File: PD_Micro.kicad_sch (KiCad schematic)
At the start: 43 parts, among them J3 Conn_01x02, Q1 DMP3017SFK, Q2 DTC143E, SW1 SW_DPST_x2, SW2 SW_Push, SW4 SW_DPST_x2, SW5 SW_DIP_x06, SW6 SW_Push, U1 TPS62175DQC, U2 SRV05-4, U3 Pico, U4 FUSB302BMPX, U5 ACS723xMATR-10AB, U6 oledSym

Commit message: pcb
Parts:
- SW2, SW6: footprint Button_Switch_SMD:SW_SPST_TL3305C -> Button_Switch_SMD:SW_SPST_TL3305B
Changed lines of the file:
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@@
       (effects (font (size 1.27 1.27)))
     )
-    (property "Footprint" "Button_Switch_SMD:SW_SPST_TL3305C" (at 118.11 144.78 0)
+    (property "Footprint" "Button_Switch_SMD:SW_SPST_TL3305B" (at 118.11 144.78 0)
       (effects (font (size 1.27 1.27)) hide)
     )
@@
       (effects (font (size 1.27 1.27)))
     )
-    (property "Footprint" "Button_Switch_SMD:SW_SPST_TL3305C" (at 116.84 134.62 0)
+    (property "Footprint" "Button_Switch_SMD:SW_SPST_TL3305B" (at 116.84 134.62 0)
       (effects (font (size 1.27 1.27)) hide)
     )

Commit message: silk
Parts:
- renumbered C12 to C1, C13 to C10, C1 to C11, C15 to C12, C6 to C2, C16 to C3, C8 to C4, C17 to C5, C7 to C6, C4 to C7, C3 to C8, C2 to C9, H3 to H1, H1 to H2, H4 to H3, H2 to H4, J3 to J1, R9 to R1, R8 to R2, R7 to R3, R12 to R4, R4 to R5, R1 to R6, R2 to R7, R3 to R8, R11 to R9, SW5 to SW1, SW1 to SW2, SW6 to SW3, SW2 to SW4, SW4 to SW5, U2 to U1, U3 to U2, U1 to U3
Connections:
- net GND: now also U2.33 (AGND)

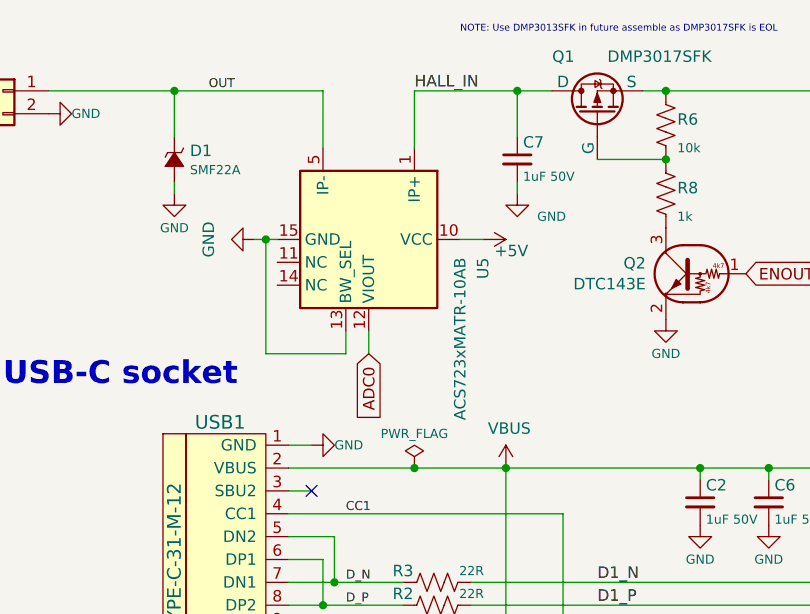
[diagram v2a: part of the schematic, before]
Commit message: bevore silkscreen delete
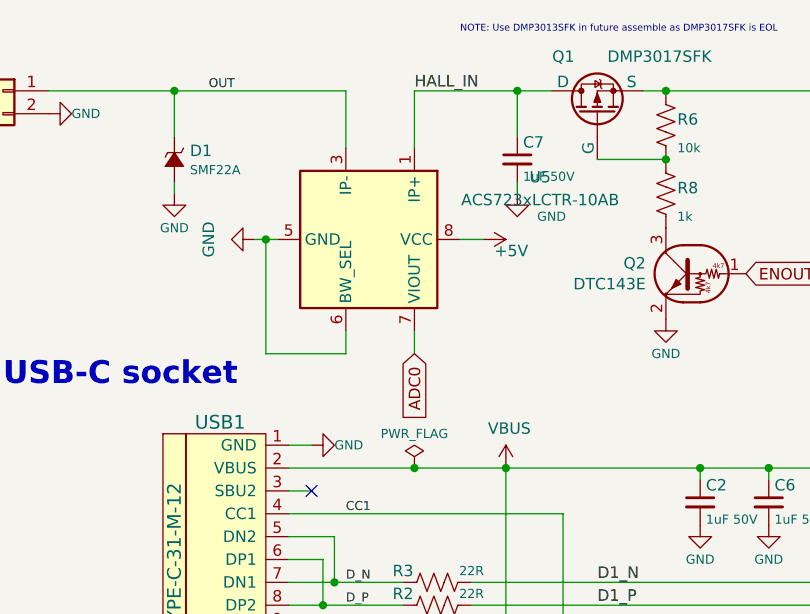
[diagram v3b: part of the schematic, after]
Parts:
- removed U5: ACS723xMATR-10AB, Package_SO:SOIC-16W_7.5x10.3mm_P1.27mm, symbol Sensor_Current:ACS723xMATR-10AB
- added U5: ACS723xLCTR-10AB, Package_SO:SOIC-8_3.9x4.9mm_P1.27mm, symbol Sensor_Current:ACS723xLCTR-10AB
- U6: footprint SSD1306:128x64OLED -> OLED094:SSD1306_0.96_Oled
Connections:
- net +5V: now also U5.8 (VCC)
- net ADC0: now also U5.7 (VIOUT)
- net GND: now also U5.5 (GND), U5.6 (BW_SEL)
- net HALL_IN: now also U5.1 (IP+), U5.2 (IP+)
- net OUT: now also U5.3 (IP-), U5.4 (IP-)
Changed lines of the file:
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@@
     (stroke (width 0) (type default))
   )
-  (wire (pts (xy 49.53 22.86) (xy 66.04 22.86))
+  (wire (pts (xy 49.53 22.86) (xy 68.58 22.86))
     (stroke (width 0) (type default))
   )
@@
     (stroke (width 0) (type default))
   )
-  (wire (pts (xy 66.04 29.21) (xy 66.04 22.86))
+  (wire (pts (xy 68.58 29.21) (xy 68.58 22.86))
     (stroke (width 0) (type default))
   )
@@
     (stroke (width 0) (type default))
   )
-  (wire (pts (xy 71.12 49.53) (xy 71.12 52.07))
+  (wire (pts (xy 76.2 49.53) (xy 76.2 52.07))
     (stroke (width 0) (type default))
   )
@@
     )
   )
-  (global_label "ADC0" (shape input) (at 71.12 52.07 270) (fields_autoplaced)
+  (global_label "ADC0" (shape input) (at 76.2 52.07 270) (fields_autoplaced)
     (effects (font (size 1.27 1.27)) (justify right))
-    (property "Intersheetrefs" "${INTERSHEET_REFS}" (at 71.1994 59.2323 90)
+    (property "Intersheetrefs" "${INTERSHEET_REFS}" (at 76.2794 59.2323 90)
       (effects (font (size 1.27 1.27)) (justify right) hide)
     )
@@
       (effects (font (size 1.27 1.27)) (justify left))
     )
-    (property "Footprint" "SSD1306:128x64OLED" (at 245.11 142.24 0)
+    (property "Footprint" "OLED094:SSD1306_0.96_Oled" (at 245.11 142.24 0)
       (effects (font (size 1.27 1.27)) hide)
     )
@@
     )
   )
-  (symbol (lib_id "Sensor_Current:ACS723xMATR-10AB") (at 71.12 39.37 270) (unit 1)
+  (symbol (lib_id "Sensor_Current:ACS723xLCTR-10AB") (at 71.12 39.37 270) (unit 1)
     (in_bom yes) (on_board yes) (dnp no) (fields_autoplaced)
-    (property "Reference" "U5" (at 83.82 41.3894 0)
-      (effects (font (size 1.27 1.27)) (justify left))
-    )
-    (property "Value" "ACS723xMATR-10AB" (at 81.28 41.3894 0)
-      (effects (font (size 1.27 1.27)) (justify left))
-    )
-    (property "Footprint" "Package_SO:SOIC-16W_7.5x10.3mm_P1.27mm" (at 69.85 48.26 0)
+    (property "Reference" "U5" (at 90.17 32.4419 90)
+      (effects (font (size 1.27 1.27)))
+    )
+    (property "Value" "ACS723xLCTR-10AB" (at 90.17 34.9819 90)
+      (effects (font (size 1.27 1.27)))
+    )
+    (property "Footprint" "Package_SO:SOIC-8_3.9x4.9mm_P1.27mm" (at 62.23 41.91 0)
       (effects (font (size 1.27 1.27) italic) (justify left) hide)
     )
-    (property "Datasheet" "http://www.allegromicro.com/~/media/Files/Datasheets/ACS723KMA-Datasheet.ashx?la=en" (at 71.12 39.37 0)
-      (effects (font (size 1.27 1.27)) hide)
-    )
-    (pin "1")
-    (pin "10")
-    (pin "11")
-    (pin "12")
-    (pin "13")
-    (pin "14")
-    (pin "15")
-    (pin "16")
+    (property "Datasheet" "http://www.allegromicro.com/~/media/Files/Datasheets/ACS723-Datasheet.ashx?la=en" (at 71.12 39.37 0)
+      (effects (font (size 1.27 1.27)) hide)
+    )
+    (pin "1")
     (pin "2")
     (pin "3")
@@
     (pin "7")
     (pin "8")
-    (pin "9")
-    (instances
-      (project "PD_Micro"
+    (instances
+      (project "PD_Micro"

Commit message: schematic finished
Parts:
- removed C12: 0.1uF, Capacitor_SMD:C_0805_2012Metric, symbol -Passive:C
- removed C5: 330pF, Capacitor_SMD:C_0805_2012Metric, symbol -Passive:C
- removed U4: FUSB302BMPX, -Chip:WQFN-14-1EP_2.5x2.5mm_P0.5mm_EP1.45x1.45mm, symbol -Chip:FUSB302BMPX
- added C13: 100nF, Package_DFN_QFN:WQFN-24-1EP_4x4mm_P0.5mm_EP2.6x2.6mm, symbol -Passive:C
- added C14: 1uF, Capacitor_SMD:C_0805_2012Metric, symbol -Passive:C
- added C15: 100nF, Capacitor_SMD:C_0805_2012Metric, symbol -Passive:C
- added C16: 2.2u, Capacitor_SMD:C_0805_2012Metric, symbol -Passive:C
- added J2, J3, J4, J5: Conn_01x02, symbol -Connector:Conn_01x02
- added L2: 10uH, -Passive:L_4012, symbol -Passive:L_cored
- added R10, R11: 5.1k, symbol -Passive:R
- added R12: 270k, Resistor_SMD:R_0805_2012Metric, symbol -Passive:R
- added R13: 100k, symbol -Passive:R
- added R14: 51k, Resistor_SMD:R_0805_2012Metric, symbol -Passive:R
- added TH1: Thermistor, symbol Device:Thermistor
- added TP1, TP2: TestPoint, symbol -Connector:TestPoint
- added U4: TPS62175DQC, -Chip:WSON-10-1EP_2x3mm_P0.5mm_EP0.84x2.4mm, symbol -Chip:TPS62175DQC
- added U7: ~, Package_DFN_QFN:WQFN-24-1EP_4x4mm_P0.5mm_EP2.6x2.6mm, symbol AP33772:AP33772
- C3: value 330pF -> 22u
- R4, R9: value 2k -> 5.1k
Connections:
- net +5V: now also J4.1 (Pin_1), J4.2 (Pin_2), U4.8 (~{SLEEP}); no longer R4.1, R9.1
- net CC1: now also R11.1, TP1.1, U7.17 (CC1)
- net CC2: now also R10.1, TP2.1, U7.16 (CC2); no longer C3.2
- net GND: now also C3.2, C13.2, C14.2, C15.2, C16.2, J5.1 (Pin_1), J5.2 (Pin_2), R10.2, R11.2, R14.2, TH1.2, U4.1 (PGND), U4.11 (PAD), U4.4 (NC), U4.6 (AGND), U7.25 (EP), U7.3 (GND); no longer C3.1
- net SCL: now also U7.5 (SCL)
- net SDA: now also U7.4 (SDA)
- net SW1: now also L2.1, U4.9 (SW)
- net VBUS: now also C16.1, J2.1 (Pin_1), J2.2 (Pin_2), U4.2 (VIN), U4.3 (EN), U7.1 (ISENP), U7.22 (VBUS), U7.24 (VCC)
- new net: R13.1, U4.7 (PG)
- new net: R12.2, R14.1, U4.5 (FB)
- new net: C14.1, U7.20 (VSV)
- new net: C13.1, U7.15 (IFB)
- new net: C15.1, U7.12 (V3VD)
- new net: TH1.1, U7.13 (OTP)
- new net +3.3V: C3.1, J3.1 (Pin_1), J3.2 (Pin_2), L2.2, R12.1, R13.2, R4.1, R9.1, U4.10 (VOS)
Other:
- note removed: "I2C Address: 0x22"
- moved on the sheet: SW1

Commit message: sch finished, parts placed
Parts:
- added TP3: TestPoint, TestPoint:TestPoint_Pad_D1.0mm, symbol -Connector:TestPoint
- C13: footprint Package_DFN_QFN:WQFN-24-1EP_4x4mm_P0.5mm_EP2.6x2.6mm -> Capacitor_SMD:C_0805_2012Metric
- J2, J3, J4, J5: footprint (none) -> Connector_PinHeader_1.00mm:PinHeader_1x02_P1.00mm_Vertical
- R10, R11, R13, TH1: footprint (none) -> Resistor_SMD:R_0805_2012Metric
- R14: value 51k -> 30k
- TP1, TP2: footprint (none) -> Connector_PinHeader_1.00mm:PinHeader_1x01_P1.00mm_Vertical
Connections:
- net at Q1.3 (G), R6.2, R8.1: now also TP3.1
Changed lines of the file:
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@@
     (stroke (width 0) (type default))
   )
+  (wire (pts (xy 104.14 30.48) (xy 111.76 30.48))
+    (stroke (width 0) (type default))
+  )
   (wire (pts (xy 167.64 165.1) (xy 171.45 165.1))
     (stroke (width 0) (type default))
@@
     (stroke (width 0) (type default))
   )
+  (wire (pts (xy 111.76 30.48) (xy 111.76 29.21))
+    (stroke (width 0) (type default))
+  )
   (wire (pts (xy 186.69 22.86) (xy 194.31 22.86))
     (stroke (width 0) (type default))
@@
       (effects (font (size 1.27 1.27)) (justify left))
     )
-    (property "Footprint" "" (at 194.31 74.93 0)
+    (property "Footprint" "Connector_PinHeader_1.00mm:PinHeader_1x01_P1.00mm_Vertical" (at 194.31 74.93 0)
       (effects (font (size 1.27 1.27)) hide)
     )
@@
       (effects (font (size 1.016 1.016)))
     )
-    (property "Footprint" "" (at 222.504 66.294 90)
+    (property "Footprint" "Resistor_SMD:R_0805_2012Metric" (at 222.504 66.294 90)
       (effects (font (size 1.27 1.27)) hide)
     )
@@
       (effects (font (size 1.27 1.27)) (justify left))
     )
-    (property "Footprint" "" (at 196.85 74.93 0)
+    (property "Footprint" "Connector_PinHeader_1.00mm:PinHeader_1x01_P1.00mm_Vertical" (at 196.85 74.93 0)
       (effects (font (size 1.27 1.27)) hide)
     )
@@
     )
   )
+  (symbol (lib_id "-Connector:TestPoint") (at 111.76 29.21 0) (unit 1)
+    (in_bom yes) (on_board yes) (dnp no) (fields_autoplaced)
+    (property "Reference" "TP3" (at 114.3 24.638 0)
+      (effects (font (size 1.27 1.27)) (justify left))
+    )
+    (property "Value" "TestPoint" (at 114.3 27.178 0)
+      (effects (font (size 1.27 1.27)) (justify left))
+    )
+    (property "Footprint" "TestPoint:TestPoint_Pad_D1.0mm" (at 116.84 29.21 0)
+      (effects (font (size 1.27 1.27)) hide)
+    )
+    (property "Datasheet" "" (at 116.84 29.21 0)
+      (effects (font (size 1.27 1.27)) hide)
+    )
+    (pin "1")
+    (instances
+      (project "PD_Micro"
+        (path "/e63e39d7-6ac0-4ffd-8aa3-1841a4541b55"
+          (reference "TP3") (unit 1)
+        )
+      )
+    )
+  )
   (symbol (lib_name "C_1") (lib_id "-Passive:C") (at 240.03 110.49 0) (unit 1)
     (in_bom yes) (on_board yes) (dnp no)
@@
       (effects (font (size 1.016 1.016)) (justify left))
     )
-    (property "Footprint" "Package_DFN_QFN:WQFN-24-1EP_4x4mm_P0.5mm_EP2.6x2.6mm" (at 240.03 110.49 0)
+    (property "Footprint" "Capacitor_SMD:C_0805_2012Metric" (at 240.03 110.49 0)
       (effects (font (size 1.27 1.27)) hide)
     )
@@
       (effects (font (size 1.016 1.016)))
     )
-    (property "Footprint" "" (at 99.314 127.254 90)
+    (property "Footprint" "Resistor_SMD:R_0805_2012Metric" (at 99.314 127.254 90)
       (effects (font (size 1.27 1.27)) hide)
     )
@@
       (effects (font (size 1.27 1.27)) (justify left))
     )
-    (property "Footprint" "" (at 144.78 69.85 0)
+    (property "Footprint" "Connector_PinHeader_1.00mm:PinHeader_1x02_P1.00mm_Vertical" (at 144.78 69.85 0)
       (effects (font (size 1.27 1.27)) hide)
     )
@@
       (effects (font (size 1.27 1.27)) (justify left))
     )
-    (property "Value" "51k" (at 245.11 55.88 0)
+    (property "Value" "30k" (at 245.11 55.88 0)
       (effects (font (size 1.016 1.016)) (justify left))
     )
@@
       (effects (font (size 1.27 1.27)) (justify left))
     )
-    (property "Footprint" "" (at 144.78 82.55 0)
+    (property "Footprint" "Connector_PinHeader_1.00mm:PinHeader_1x02_P1.00mm_Vertical" (at 144.78 82.55 0)
       (effects (font (size 1.27 1.27)) hide)
     )
@@
       (effects (font (size 1.27 1.27)) (justify left))
     )
-    (property "Footprint" "" (at 228.6 113.03 0)
+    (property "Footprint" "Resistor_SMD:R_0805_2012Metric" (at 228.6 113.03 0)
       (effects (font (size 1.27 1.27)) hide)
     )
@@
       (effects (font (size 1.27 1.27)) (justify left))
     )
-    (property "Footprint" "" (at 144.78 76.2 0)
+    (property "Footprint" "Connector_PinHeader_1.00mm:PinHeader_1x02_P1.00mm_Vertical" (at 144.78 76.2 0)
       (effects (font (size 1.27 1.27)) hide)
     )
@@
       (effects (font (size 1.27 1.27)) (justify left))
     )
-    (property "Footprint" "" (at 144.78 63.5 0)
+    (property "Footprint" "Connector_PinHeader_1.00mm:PinHeader_1x02_P1.00mm_Vertical" (at 144.78 63.5 0)
       (effects (font (size 1.27 1.27)) hide)
     )
@@
       (effects (font (size 1.016 1.016)))
     )
-    (property "Footprint" "" (at 99.314 117.094 90)
+    (property "Footprint" "Resistor_SMD:R_0805_2012Metric" (at 99.314 117.094 90)
       (effects (font (size 1.27 1.27)) hide)
     )

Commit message: v2.1
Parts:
- removed TP3: TestPoint, TestPoint:TestPoint_Pad_D1.0mm, symbol -Connector:TestPoint
- added C5: 2.2u, Capacitor_SMD:C_0805_2012Metric, symbol -Passive:C
- added R15: 100k, Resistor_SMD:R_0805_2012Metric, symbol -Passive:R
- U7: footprint Package_DFN_QFN:WQFN-24-1EP_4x4mm_P0.5mm_EP2.6x2.6mm -> Package_DFN_QFN:WQFN-24-1EP_4x4mm_P0.5mm_EP2.6x2.6mm_ThermalVias
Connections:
- net +5V: now also R15.2
- net GND: now also C5.2
- net VBUS: now also C5.1
- net at U3.7 (PG): now also R15.1
- net SW1: no longer names the net of L1.1, U3.9 (SW)
- net SW1: no longer L2.1, U4.9 (SW)
- new net: L2.1, U4.9 (SW)
- no-connect marks 3 -> 2
